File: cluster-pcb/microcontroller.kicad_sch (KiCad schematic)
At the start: 4 parts

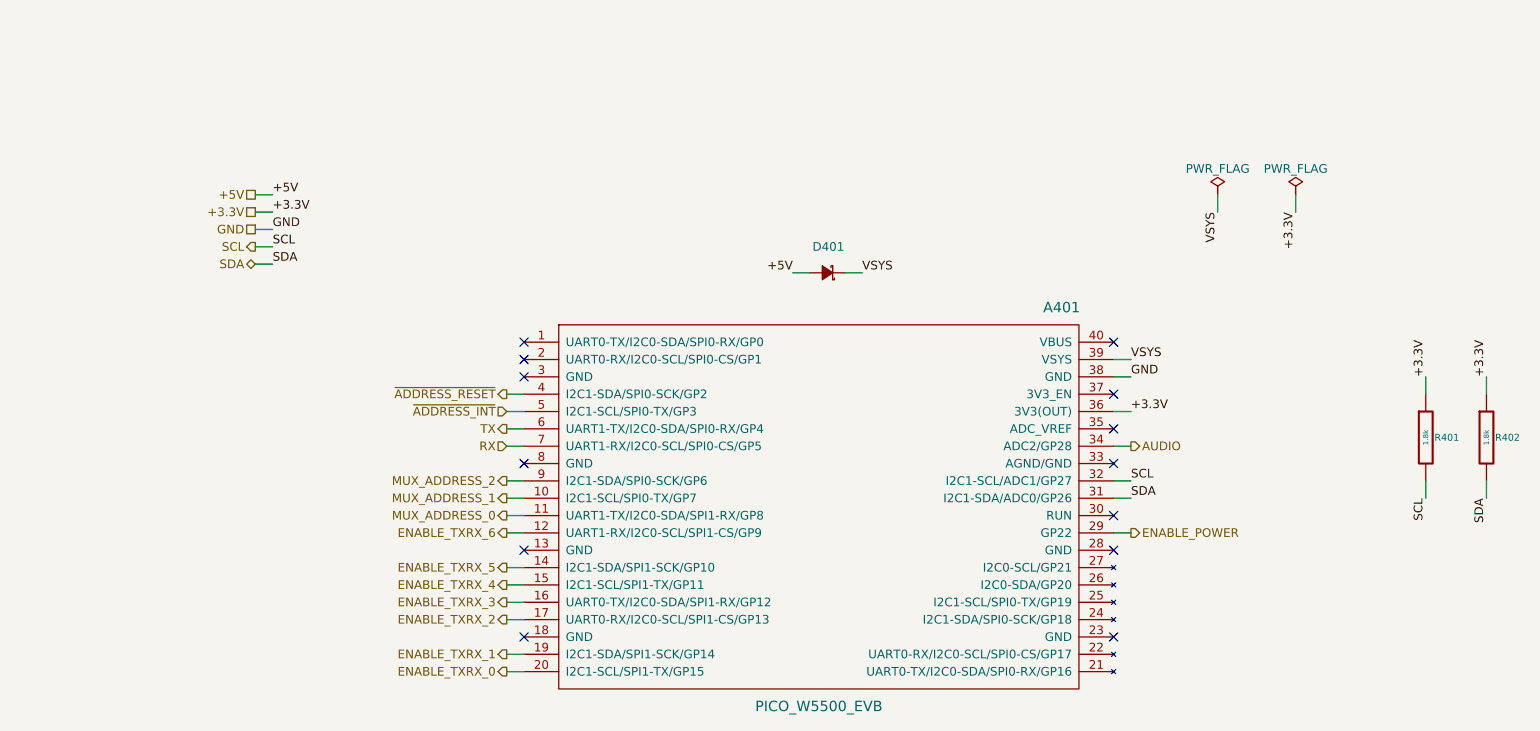
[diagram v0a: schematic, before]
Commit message: Routed most tracks
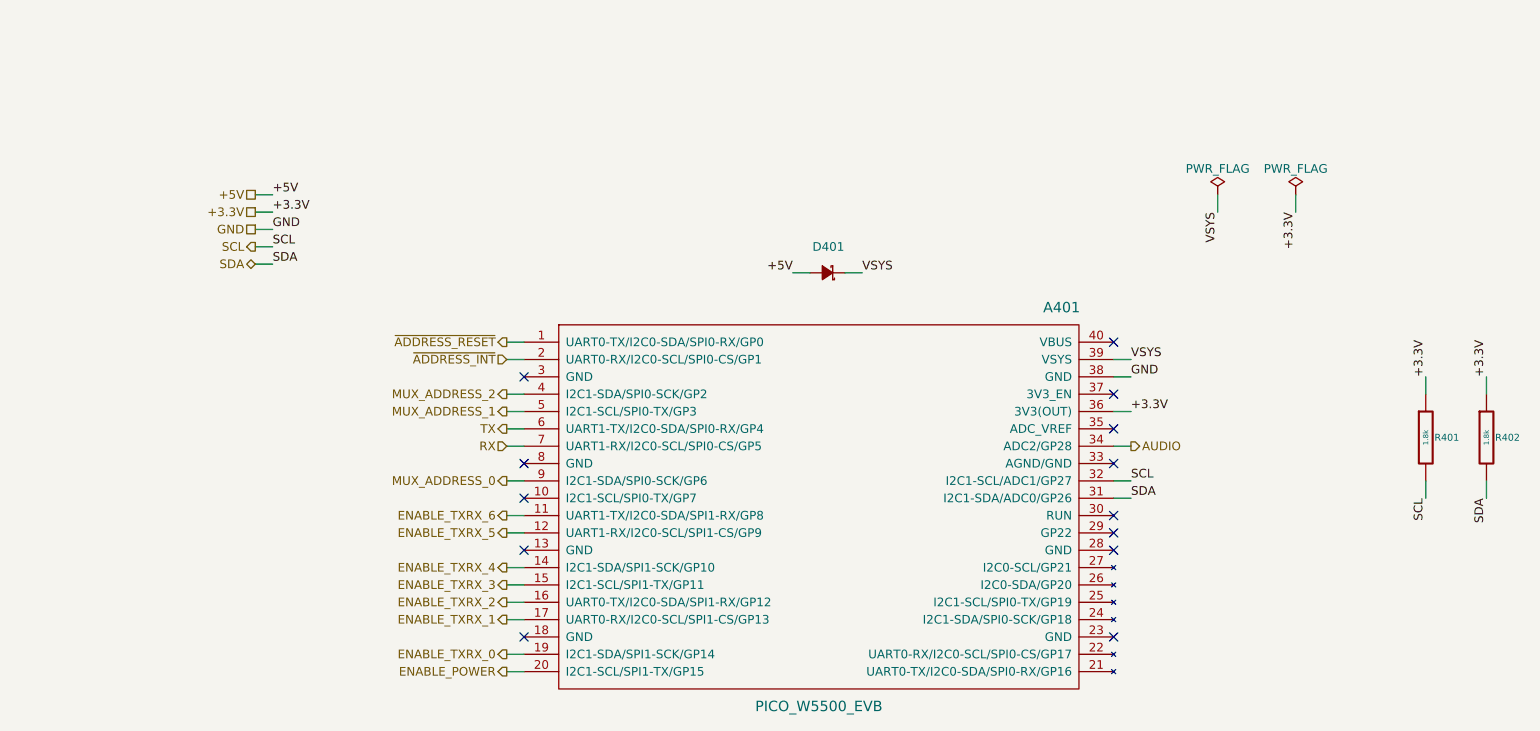
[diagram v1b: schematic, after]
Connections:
- net ENABLE_POWER: now also A401.20 (I2C1-SCL/SPI1-TX/GP15); no longer A401.29 (GP22)
- net ENABLE_TXRX_0: now also A401.19 (I2C1-SDA/SPI1-SCK/GP14); no longer A401.20 (I2C1-SCL/SPI1-TX/GP15)
- net ENABLE_TXRX_1: now also A401.17 (UART0-RX/I2C0-SCL/SPI1-CS/GP13); no longer A401.19 (I2C1-SDA/SPI1-SCK/GP14)
- net ENABLE_TXRX_2: now also A401.16 (UART0-TX/I2C0-SDA/SPI1-RX/GP12); no longer A401.17 (UART0-RX/I2C0-SCL/SPI1-CS/GP13)
- net ENABLE_TXRX_3: now also A401.15 (I2C1-SCL/SPI1-TX/GP11); no longer A401.16 (UART0-TX/I2C0-SDA/SPI1-RX/GP12)
- net ENABLE_TXRX_4: now also A401.14 (I2C1-SDA/SPI1-SCK/GP10); no longer A401.15 (I2C1-SCL/SPI1-TX/GP11)
- net ENABLE_TXRX_5: now also A401.12 (UART1-RX/I2C0-SCL/SPI1-CS/GP9); no longer A401.14 (I2C1-SDA/SPI1-SCK/GP10)
- net ENABLE_TXRX_6: now also A401.11 (UART1-TX/I2C0-SDA/SPI1-RX/GP8); no longer A401.12 (UART1-RX/I2C0-SCL/SPI1-CS/GP9)
- net MUX_ADDRESS_0: now also A401.9 (I2C1-SDA/SPI0-SCK/GP6); no longer A401.11 (UART1-TX/I2C0-SDA/SPI1-RX/GP8)
- net MUX_ADDRESS_1: now also A401.5 (I2C1-SCL/SPI0-TX/GP3); no longer A401.10 (I2C1-SCL/SPI0-TX/GP7)
- net MUX_ADDRESS_2: now also A401.4 (I2C1-SDA/SPI0-SCK/GP2); no longer A401.9 (I2C1-SDA/SPI0-SCK/GP6)
- net ~{ADDRESS_INT}: now also A401.2 (UART0-RX/I2C0-SCL/SPI0-CS/GP1); no longer A401.5 (I2C1-SCL/SPI0-TX/GP3)
- net ~{ADDRESS_RESET}: now also A401.1 (UART0-TX/I2C0-SDA/SPI0-RX/GP0); no longer A401.4 (I2C1-SDA/SPI0-SCK/GP2)
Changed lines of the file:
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@@
   )
   (no_connect (at 180.34 81.28))
-  (no_connect (at 93.98 71.12))
   (no_connect (at 180.34 99.06))
   (no_connect (at 93.98 86.36))
@@
   (no_connect (at 180.34 111.76))
   (no_connect (at 180.34 76.2))
-  (no_connect (at 93.98 68.58))
+  (no_connect (at 93.98 91.44))
+  (no_connect (at 180.34 96.52))
   (no_connect (at 93.98 99.06))
   (no_connect (at 93.98 73.66))
@@
     (stroke (width 0) (type default))
   )
-  (wire (pts (xy 180.34 96.52) (xy 182.88 96.52))
+  (wire (pts (xy 91.44 76.2) (xy 93.98 76.2))
     (stroke (width 0) (type default))
   )
@@
     (stroke (width 0) (type default))
   )
-  (wire (pts (xy 91.44 76.2) (xy 93.98 76.2))
+  (wire (pts (xy 91.44 68.58) (xy 93.98 68.58))
     (stroke (width 0) (type default))
   )
@@
     (stroke (width 0) (type default))
   )
-  (wire (pts (xy 91.44 91.44) (xy 93.98 91.44))
+  (wire (pts (xy 91.44 78.74) (xy 93.98 78.74))
     (stroke (width 0) (type default))
   )
@@
     (stroke (width 0) (type default))
   )
-  (wire (pts (xy 91.44 78.74) (xy 93.98 78.74))
+  (wire (pts (xy 91.44 71.12) (xy 93.98 71.12))
     (stroke (width 0) (type default))
   )
@@
     (effects (font (size 1.27 1.27)) (justify left))
   )
-  (hierarchical_label "ENABLE_POWER" (shape output) (at 182.88 96.52 0) (fields_autoplaced)
-    (effects (font (size 1.27 1.27)) (justify left))
-  )
-  (hierarchical_label "~{ADDRESS_INT}" (shape input) (at 91.44 78.74 180) (fields_autoplaced)
-    (effects (font (size 1.27 1.27)) (justify right))
-  )
-  (hierarchical_label "ENABLE_TXRX_2" (shape output) (at 91.44 109.22 180) (fields_autoplaced)
+  (hierarchical_label "ENABLE_POWER" (shape output) (at 91.44 116.84 180) (fields_autoplaced)
+    (effects (font (size 1.27 1.27)) (justify right))
+  )
+  (hierarchical_label "~{ADDRESS_INT}" (shape input) (at 91.44 71.12 180) (fields_autoplaced)
+    (effects (font (size 1.27 1.27)) (justify right))
+  )
+  (hierarchical_label "ENABLE_TXRX_2" (shape output) (at 91.44 106.68 180) (fields_autoplaced)
     (effects (font (size 1.27 1.27)) (justify right))
   )
@@
     (effects (font (size 1.27 1.27)) (justify right))
   )
-  (hierarchical_label "ENABLE_TXRX_6" (shape output) (at 91.44 96.52 180) (fields_autoplaced)
-    (effects (font (size 1.27 1.27)) (justify right))
-  )
-  (hierarchical_label "MUX_ADDRESS_0" (shape output) (at 91.44 93.98 180) (fields_autoplaced)
+  (hierarchical_label "ENABLE_TXRX_6" (shape output) (at 91.44 93.98 180) (fields_autoplaced)
+    (effects (font (size 1.27 1.27)) (justify right))
+  )
+  (hierarchical_label "MUX_ADDRESS_0" (shape output) (at 91.44 88.9 180) (fields_autoplaced)
     (effects (font (size 1.27 1.27)) (justify right))
   )
@@
     (effects (font (size 1.27 1.27)) (justify right))
   )
-  (hierarchical_label "~{ADDRESS_RESET}" (shape output) (at 91.44 76.2 180) (fields_autoplaced)
-    (effects (font (size 1.27 1.27)) (justify right))
-  )
-  (hierarchical_label "ENABLE_TXRX_1" (shape output) (at 91.44 114.3 180) (fields_autoplaced)
-    (effects (font (size 1.27 1.27)) (justify right))
-  )
-  (hierarchical_label "ENABLE_TXRX_0" (shape output) (at 91.44 116.84 180) (fields_autoplaced)
-    (effects (font (size 1.27 1.27)) (justify right))
-  )
-  (hierarchical_label "ENABLE_TXRX_3" (shape output) (at 91.44 106.68 180) (fields_autoplaced)
-    (effects (font (size 1.27 1.27)) (justify right))
-  )
-  (hierarchical_label "ENABLE_TXRX_5" (shape output) (at 91.44 101.6 180) (fields_autoplaced)
+  (hierarchical_label "~{ADDRESS_RESET}" (shape output) (at 91.44 68.58 180) (fields_autoplaced)
+    (effects (font (size 1.27 1.27)) (justify right))
+  )
+  (hierarchical_label "ENABLE_TXRX_1" (shape output) (at 91.44 109.22 180) (fields_autoplaced)
+    (effects (font (size 1.27 1.27)) (justify right))
+  )
+  (hierarchical_label "ENABLE_TXRX_0" (shape output) (at 91.44 114.3 180) (fields_autoplaced)
+    (effects (font (size 1.27 1.27)) (justify right))
+  )
+  (hierarchical_label "ENABLE_TXRX_3" (shape output) (at 91.44 104.14 180) (fields_autoplaced)
+    (effects (font (size 1.27 1.27)) (justify right))
+  )
+  (hierarchical_label "ENABLE_TXRX_5" (shape output) (at 91.44 96.52 180) (fields_autoplaced)
     (effects (font (size 1.27 1.27)) (justify right))
   )
@@
     (effects (font (size 1.27 1.27)) (justify right))
   )
-  (hierarchical_label "ENABLE_TXRX_4" (shape output) (at 91.44 104.14 180) (fields_autoplaced)
-    (effects (font (size 1.27 1.27)) (justify right))
-  )
-  (hierarchical_label "MUX_ADDRESS_2" (shape output) (at 91.44 88.9 180) (fields_autoplaced)
+  (hierarchical_label "ENABLE_TXRX_4" (shape output) (at 91.44 101.6 180) (fields_autoplaced)
+    (effects (font (size 1.27 1.27)) (justify right))
+  )
+  (hierarchical_label "MUX_ADDRESS_2" (shape output) (at 91.44 76.2 180) (fields_autoplaced)
     (effects (font (size 1.27 1.27)) (justify right))
   )
@@
     (effects (font (size 1.27 1.27)) (justify right))
   )
-  (hierarchical_label "MUX_ADDRESS_1" (shape output) (at 91.44 91.44 180) (fields_autoplaced)
-    (effects (font (size 1.27 1.27)) (justify right))
-  )
+  (hierarchical_label "MUX_ADDRESS_1" (shape output) (at 91.44 78.74 180) (fields_autoplaced)
+    (effects (font (size 1.27 1.27)) (justify right))
+  )

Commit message: Progress toward v2.0
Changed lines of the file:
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@@
     (stroke (width 0) (type default))
   )
-  (wire (pts (xy 54.61 49.53) (xy 57.15 49.53))
+  (wire (pts (xy 27.94 25.4) (xy 30.48 25.4))
     (stroke (width 0) (type default))
   )
-  (wire (pts (xy 54.61 57.15) (xy 57.15 57.15))
+  (wire (pts (xy 27.94 33.02) (xy 30.48 33.02))
     (stroke (width 0) (type default))
   )
@@
     (stroke (width 0) (type default))
   )
-  (wire (pts (xy 54.61 52.07) (xy 57.15 52.07))
+  (wire (pts (xy 27.94 27.94) (xy 30.48 27.94))
     (stroke (width 0) (type default))
   )
@@
     (stroke (width 0) (type default))
   )
-  (wire (pts (xy 54.61 54.61) (xy 57.15 54.61))
+  (wire (pts (xy 27.94 30.48) (xy 30.48 30.48))
     (stroke (width 0) (type default))
   )
@@
     (stroke (width 0) (type default))
   )
-  (wire (pts (xy 54.61 46.99) (xy 57.15 46.99))
+  (wire (pts (xy 27.94 22.86) (xy 30.48 22.86))
     (stroke (width 0) (type default))
   )
@@
     (stroke (width 0) (type default))
   )
-  (label "+3.3V" (at 57.15 49.53 0) (fields_autoplaced)
+  (label "+3.3V" (at 30.48 25.4 0) (fields_autoplaced)
     (effects (font (size 1.27 1.27)) (justify left bottom))
   )
@@
     (effects (font (size 1.27 1.27)) (justify left bottom))
   )
-  (label "SDA" (at 57.15 57.15 0) (fields_autoplaced)
+  (label "SDA" (at 30.48 33.02 0) (fields_autoplaced)
     (effects (font (size 1.27 1.27)) (justify left bottom))
   )
@@
     (effects (font (size 1.27 1.27)) (justify left bottom))
   )
-  (label "+5V" (at 57.15 46.99 0) (fields_autoplaced)
+  (label "+5V" (at 30.48 22.86 0) (fields_autoplaced)
     (effects (font (size 1.27 1.27)) (justify left bottom))
   )
@@
     (effects (font (size 1.27 1.27)) (justify right bottom))
   )
-  (label "GND" (at 57.15 52.07 0) (fields_autoplaced)
+  (label "GND" (at 30.48 27.94 0) (fields_autoplaced)
     (effects (font (size 1.27 1.27)) (justify left bottom))
   )
-  (label "SCL" (at 57.15 54.61 0) (fields_autoplaced)
+  (label "SCL" (at 30.48 30.48 0) (fields_autoplaced)
     (effects (font (size 1.27 1.27)) (justify left bottom))
   )
@@
     (effects (font (size 1.27 1.27)) (justify right))
   )
-  (hierarchical_label "+5V" (shape passive) (at 54.61 46.99 180) (fields_autoplaced)
+  (hierarchical_label "+5V" (shape passive) (at 27.94 22.86 180) (fields_autoplaced)
     (effects (font (size 1.27 1.27)) (justify right))
   )
@@
     (effects (font (size 1.27 1.27)) (justify right))
   )
-  (hierarchical_label "GND" (shape passive) (at 54.61 52.07 180) (fields_autoplaced)
+  (hierarchical_label "GND" (shape passive) (at 27.94 27.94 180) (fields_autoplaced)
     (effects (font (size 1.27 1.27)) (justify right))
   )
@@
     (effects (font (size 1.27 1.27)) (justify right))
   )
-  (hierarchical_label "SDA" (shape bidirectional) (at 54.61 57.15 180) (fields_autoplaced)
+  (hierarchical_label "SDA" (shape bidirectional) (at 27.94 33.02 180) (fields_autoplaced)
     (effects (font (size 1.27 1.27)) (justify right))
   )
-  (hierarchical_label "SCL" (shape output) (at 54.61 54.61 180) (fields_autoplaced)
+  (hierarchical_label "SCL" (shape output) (at 27.94 30.48 180) (fields_autoplaced)
     (effects (font (size 1.27 1.27)) (justify right))
   )
@@
     (effects (font (size 1.27 1.27)) (justify right))
   )
-  (hierarchical_label "+3.3V" (shape passive) (at 54.61 49.53 180) (fields_autoplaced)
+  (hierarchical_label "+3.3V" (shape passive) (at 27.94 25.4 180) (fields_autoplaced)
     (effects (font (size 1.27 1.27)) (justify right))
   )

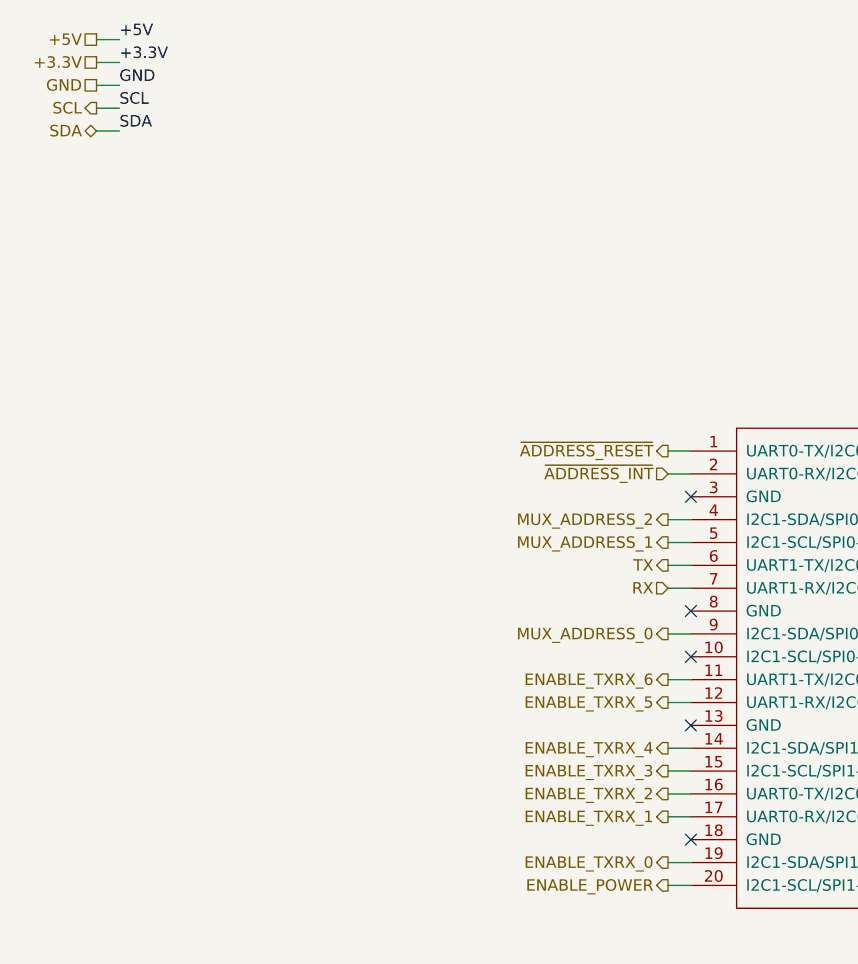
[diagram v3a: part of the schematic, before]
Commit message: Initial pcb layout
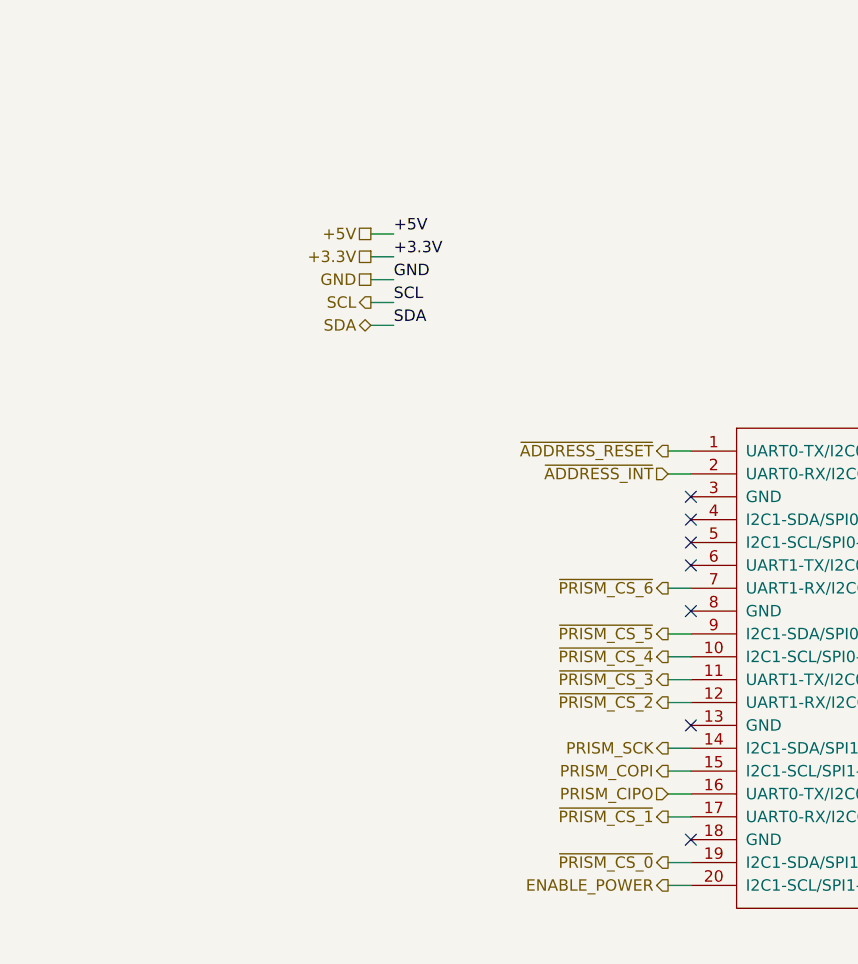
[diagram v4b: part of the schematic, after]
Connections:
- net ~{PRISM_CS_4}: now reaches A401.10 (I2C1-SCL/SPI0-TX/GP7)
- net ENABLE_TXRX_0 renamed ~{PRISM_CS_0}
- net ENABLE_TXRX_1 renamed ~{PRISM_CS_1}
- net ENABLE_TXRX_2 renamed PRISM_CIPO
- net ENABLE_TXRX_3 renamed PRISM_COPI
- net ENABLE_TXRX_4 renamed PRISM_SCK
- net ENABLE_TXRX_5 renamed ~{PRISM_CS_2}
- net ENABLE_TXRX_6 renamed ~{PRISM_CS_3}
- net MUX_ADDRESS_0 renamed ~{PRISM_CS_5}
- net MUX_ADDRESS_1: no longer names the net of A401.5 (I2C1-SCL/SPI0-TX/GP3)
- net MUX_ADDRESS_2: no longer names the net of A401.4 (I2C1-SDA/SPI0-SCK/GP2)
- net RX renamed ~{PRISM_CS_6}
- net TX: no longer names the net of A401.6 (UART1-TX/I2C0-SDA/SPI0-RX/GP4)
- no-connect marks 13 -> 15
